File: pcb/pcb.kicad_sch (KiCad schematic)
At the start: 47 parts, among them J1 Power, Q1 Q_NPN_BCE, SW1 START, SW2 RESET, U1 PIC16F18346-P, U2 74HC595, U3 SCORE 1, U4 74HC595, U5 SCORE 1, U6 SSD1306

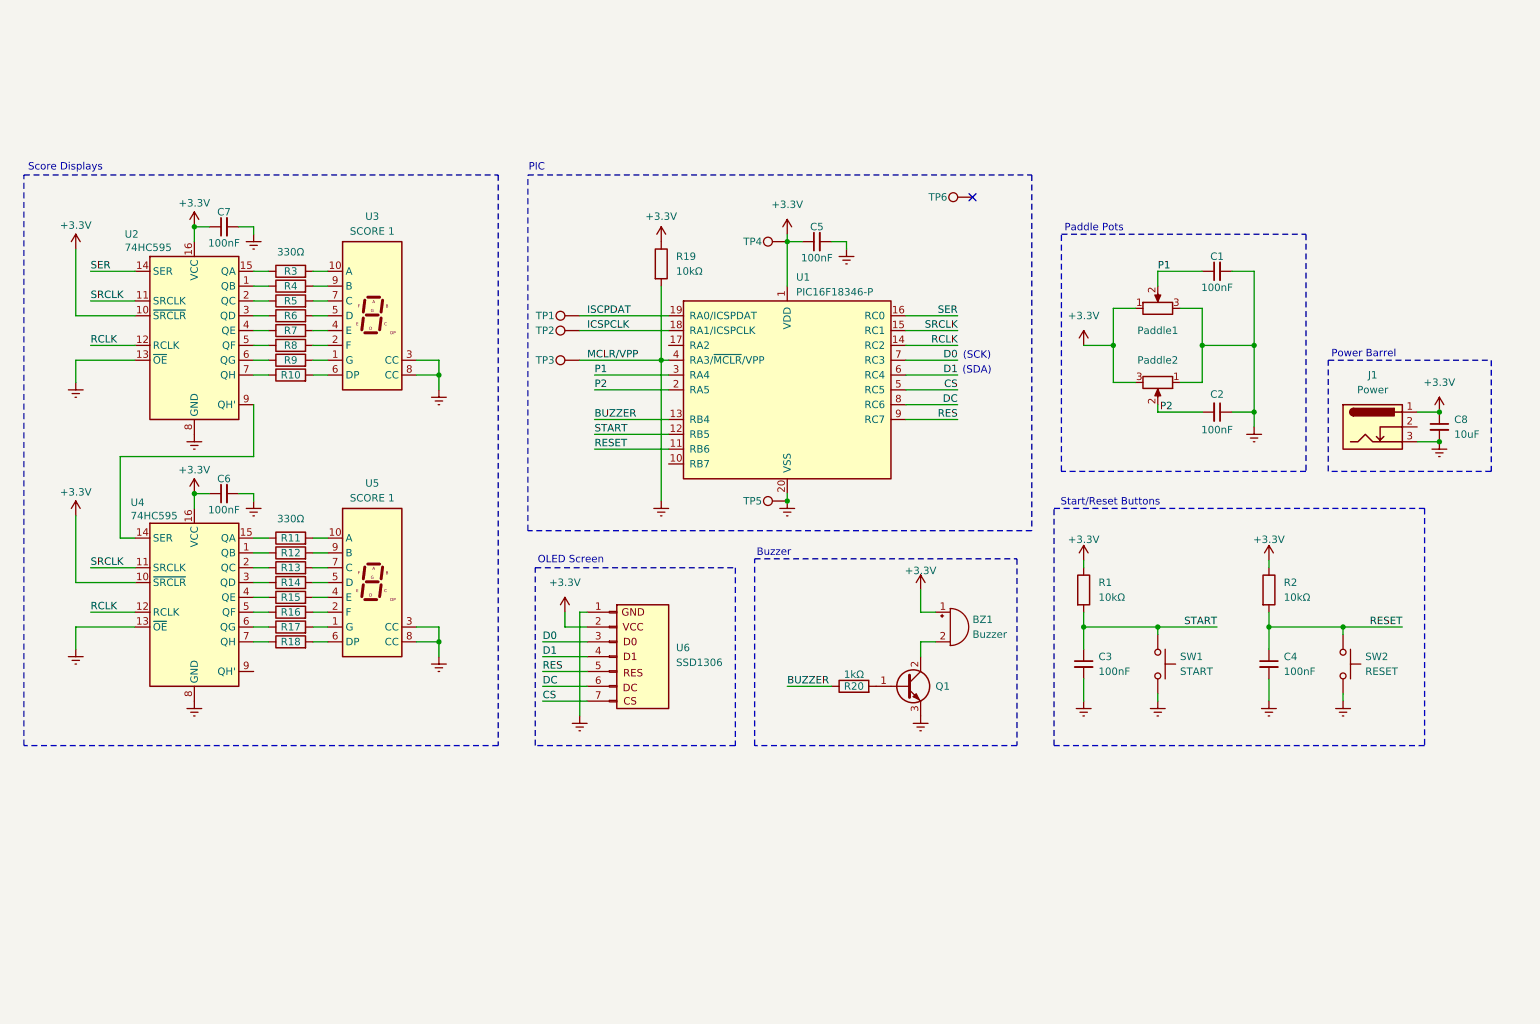
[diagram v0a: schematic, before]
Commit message: Assign footprints and start PCB
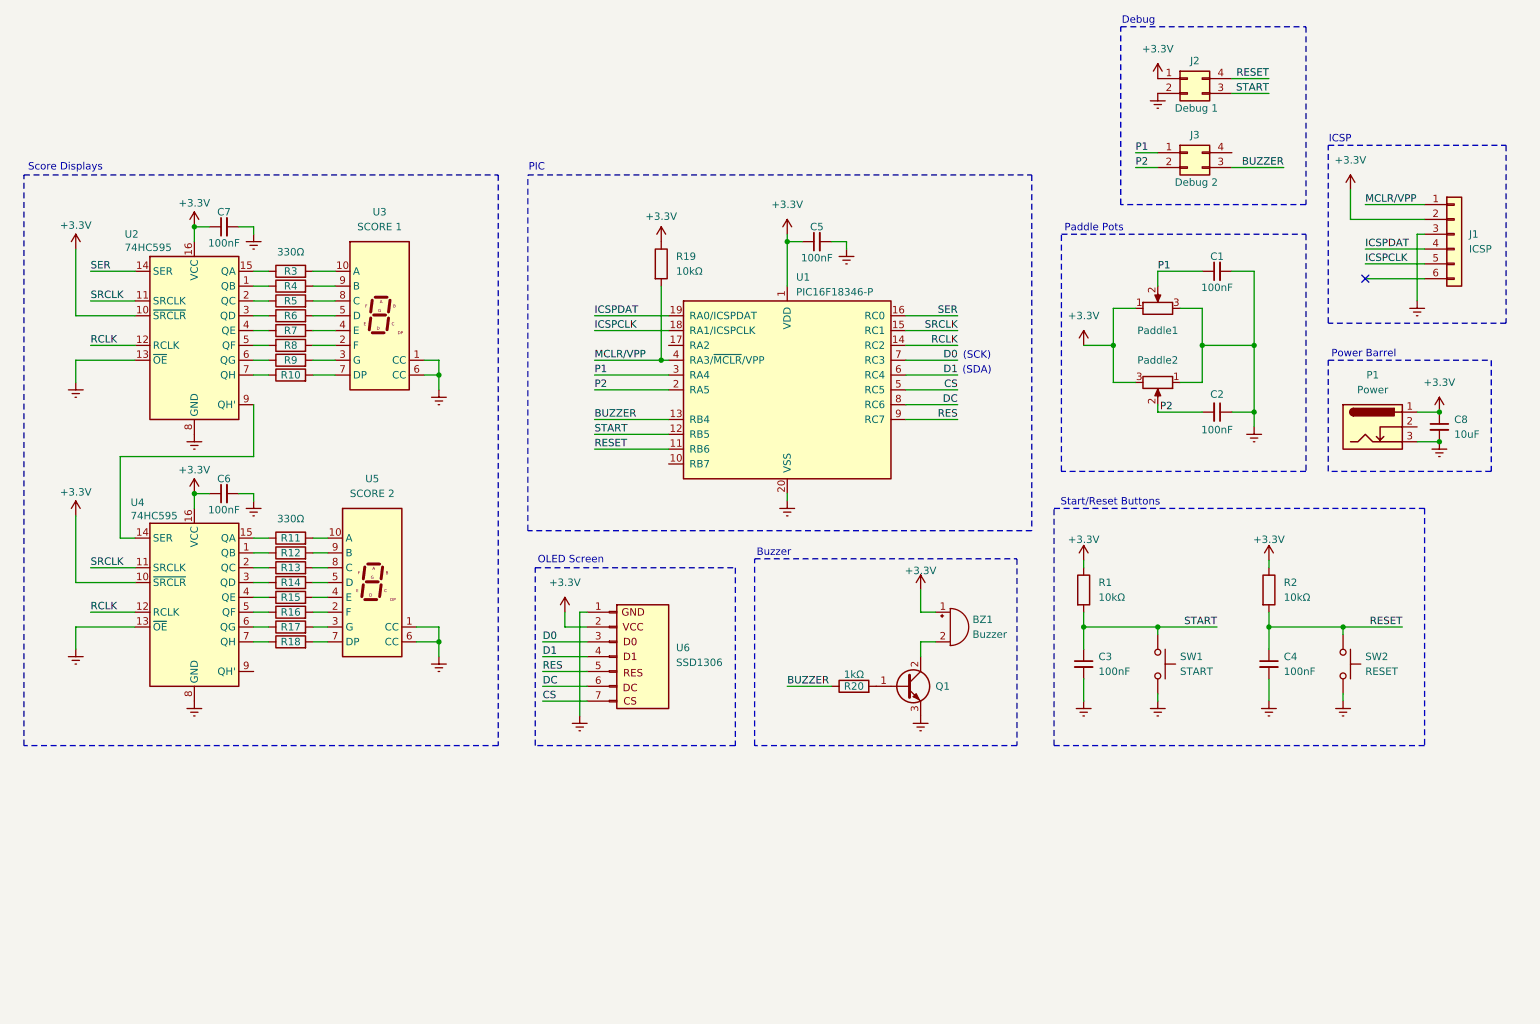
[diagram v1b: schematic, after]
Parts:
- removed TP1, TP2, TP3, TP4, TP5, TP6: TestPoint, symbol Connector:TestPoint
- added J1: ICSP, Connector_PinHeader_2.54mm:PinHeader_1x06_P2.54mm_Vertical, symbol Connector_Generic:Conn_01x06
- added J2: Debug 1, Connector_PinHeader_2.54mm:PinHeader_2x02_P2.54mm_Vertical, symbol Connector_Generic:Conn_02x02_Counter_Clockwise
- added J3: Debug 2, Connector_PinHeader_2.54mm:PinHeader_2x02_P2.54mm_Vertical, symbol Connector_Generic:Conn_02x02_Counter_Clockwise
- BZ1: footprint (none) -> Buzzer_Beeper:Buzzer_12x9.5RM7.6
- C1, C2, C3, C4, C5, C6, C7: footprint (none) -> Capacitor_THT:C_Disc_D5.0mm_W2.5mm_P5.00mm
- C8: footprint (none) -> Capacitor_THT:C_Radial_D5.0mm_H11.0mm_P2.00mm
- Paddle1, Paddle2: footprint (none) -> Potentiometer_THT:Potentiometer_Alps_RK09K_Single_Vertical
- Q1: footprint (none) -> Package_TO_SOT_THT:TO-92_Inline_Wide
- R1, R10, R11, R12, R13, R14, R15, R16, R17, R18, R19, R2, R20, R3, R4, R5, R6, R7, R8, R9: footprint (none) -> Resistor_THT:R_Axial_DIN0207_L6.3mm_D2.5mm_P10.16mm_Horizontal
- SW1, SW2: footprint (none) -> Button_Switch_THT:SW_PUSH-12mm
- U1: footprint Package_DIP:DIP-20_W7.62mm -> Package_DIP:DIP-20_W7.62mm_Socket
- U2, U4: footprint (none) -> Package_DIP:DIP-16_W7.62mm_LongPads
- U3: footprint Display_7Segment:Sx39-1xxxxx -> Display_7Segment:0.36in 3161AS
- U5: value SCORE 1 -> SCORE 2; footprint Display_7Segment:Sx39-1xxxxx -> Display_7Segment:0.36in 3161AS
- U6: footprint (none) -> Connector_PinSocket_2.54mm:PinSocket_1x07_P2.54mm_Vertical
- renumbered J1 to P1
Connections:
- net +3.3V: now also J1.2 (Pin_2), J2.1 (Pin_1)
- net BUZZER: now also J3.3 (Pin_3)
- net Earth: now also U3.1 (CC), U3.6 (CC), U5.1 (CC), U5.6 (CC), J1.3 (Pin_3), J2.2 (Pin_2); no longer R19.2, U1.4 (RA3/~{MCLR}/VPP), U3.3 (CC), U3.8 (CC), U5.3 (CC), U5.8 (CC)
- net ICSPCLK: now also J1.5 (Pin_5)
- net P1: now also J3.1 (Pin_1)
- net P2: now also J3.2 (Pin_2)
- net RESET: now also J2.4 (Pin_4)
- net START: now also J2.3 (Pin_3)
- net at R17.2: now also U5.3 (G); no longer U5.1 (G)
- net at R9.2: now also U3.3 (G); no longer U3.1 (G)
- net at R10.2: now also U3.7 (DP); no longer U3.6 (DP)
- net at R5.2: now also U3.8 (C); no longer U3.7 (C)
- net at R18.2: now also U5.7 (DP); no longer U5.6 (DP)
- net at R13.2: now also U5.8 (C); no longer U5.7 (C)
- net ISCPDAT renamed ICSPDAT
- net ICSPDAT: now also J1.4 (Pin_4)
- new net MCLR/VPP: J1.1 (Pin_1), R19.2, U1.4 (RA3/~{MCLR}/VPP)
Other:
- note added: "Debug"
- note added: "ICSP"

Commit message: Layout PCB
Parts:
- added D1: D_Small, Diode_THT:D_DO-35_SOD27_P7.62mm_Horizontal, symbol Device:D_Small
- U2, U4: footprint Package_DIP:DIP-16_W7.62mm_LongPads -> Package_DIP:DIP-16_W7.62mm_Socket_LongPads
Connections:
- net +3.3V: now also Paddle2.1, D1.1 (K); no longer Paddle2.3
- net Earth: now also Paddle2.3; no longer Paddle2.1
- net at BZ1.2 (-), Q1.2 (C): now also D1.2 (A)
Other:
- moved on the sheet: BZ1, C1, C2, C3, C4, C8, J1, J2, J3, P1, Paddle1, Paddle2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

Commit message: Hardware testing
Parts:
- removed Q1: Q_NPN_BCE, Package_TO_SOT_THT:TO-92_Inline_Wide, symbol Transistor_BJT:Q_NPN_BCE
- added Q1: BC107, Package_TO_SOT_THT:TO-92_Inline_Wide, symbol Transistor_BJT:BC107
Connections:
- net Earth: now also Q1.1 (E)
- net at R20.2: now also Q1.2 (B)
- net at BZ1.2 (-), D1.2 (A): now also Q1.3 (C)
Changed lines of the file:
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@@
 	)
 	(symbol
-		(lib_id "Transistor_BJT:Q_NPN_BCE")
-		(at 172.72 132.08 0)
-		(unit 1)
-		(exclude_from_sim no)
-		(in_bom yes)
-		(on_board yes)
-		(dnp no)
-		(property "Reference" "Q1"
-			(at 177.8 132.08 0)
-			(effects
-				(font
-					(size 1.27 1.27)
-				)
-				(justify left)
-			)
-		)
-		(property "Value" "Q_NPN_BCE"
-			(at 177.8 133.3499 0)
-			(effects
-				(font
-					(size 1.27 1.27)
-				)
-				(justify left)
-				(hide yes)
-			)
-		)
-		(property "Footprint" "Package_TO_SOT_THT:TO-92_Inline_Wide"
-			(at 177.8 129.54 0)
-			(effects
-				(font
-					(size 1.27 1.27)
-				)
-				(hide yes)
-			)
-		)
-		(property "Datasheet" "~"
-			(at 172.72 132.08 0)
-			(effects
-				(font
-					(size 1.27 1.27)
-				)
-				(hide yes)
-			)
-		)
-		(property "Description" "NPN transistor, base/collector/emitter"
-			(at 172.72 132.08 0)
-			(effects
-				(font
-					(size 1.27 1.27)
-				)
-				(hide yes)
-			)
-		)
-		(pin "2"
-		)
-		(pin "1"
-		)
-		(pin "3"
-		)
-		(instances
-			(project "pcb"
-				(path "/095fd1c6-3a4d-4d16-977e-3ab207ce523d"
-					(reference "Q1")
-					(unit 1)
-				)
-			)
-		)
-	)
-	(symbol
 		(lib_id "Device:R")
 		(at 68.58 60.96 90)
@@
 					(unit 1)
 				)
+			)
+		)
+	)
+	(symbol
+		(lib_id "Transistor_BJT:BC107")
+		(at 172.72 132.08 0)
+		(unit 1)
+		(exclude_from_sim no)
+		(in_bom yes)
+		(on_board yes)
+		(dnp no)
+		(fields_autoplaced yes)
+		(property "Reference" "Q1"
+			(at 177.8 130.8099 0)
+			(effects
+				(font
+					(size 1.27 1.27)
+				)
+				(justify left)
+			)
+		)
+		(property "Value" "BC107"
+			(at 177.8 133.3499 0)
+			(effects
+				(font
+					(size 1.27 1.27)
+				)
+				(justify left)
+			)
+		)
+		(property "Footprint" "Package_TO_SOT_THT:TO-92_Inline_Wide"
+			(at 177.8 133.985 0)
+			(effects
+				(font
+					(size 1.27 1.27)
+					(italic yes)
+				)
+				(justify left)
+				(hide yes)
+			)
+		)
+		(property "Datasheet" "http://www.b-kainka.de/Daten/Transistor/BC108.pdf"
+			(at 172.72 132.08 0)
+			(effects
+				(font
+					(size 1.27 1.27)
+				)
+				(justify left)
+				(hide yes)
+			)
+		)
+		(property "Description" "0.1A Ic, 50V Vce, Low Noise General Purpose NPN Transistor, TO-18"
+			(at 172.72 132.08 0)
+			(effects
+				(font
+					(size 1.27 1.27)
+				)
+				(hide yes)
+			)
+		)
+		(pin "3"
+		)
+		(pin "1"
+		)
+		(pin "2"
+		)
+		(instances
+			(project ""
+				(path "/095fd1c6-3a4d-4d16-977e-3ab207ce523d"
+					(reference "Q1")
+					(unit 1)
+				)

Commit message: Route PCB
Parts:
- added C9: 1uF, Capacitor_THT:C_Radial_D4.0mm_H7.0mm_P1.50mm, symbol Device:C_Small
- added U7: MCP1700x-330xxTO, Package_TO_SOT_THT:TO-92_Inline, symbol Regulator_Linear:MCP1700x-330xxTO
- C8: value 10uF -> 1uF; footprint Capacitor_THT:C_Radial_D5.0mm_H11.0mm_P2.00mm -> Capacitor_THT:C_Radial_D4.0mm_H7.0mm_P1.50mm
- Q1: value BC107 -> 2N2222
- R11, R3: value 330Ω -> 220Ω
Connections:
- net +3.3V: now also C9.1, U7.3 (VO); no longer C8.1, P1.1
- net Earth: now also P1.2, C9.2, U7.1 (GND); no longer P1.3
- net P1: now also U1.2 (RA5); no longer U1.3 (RA4)
- net P2: now also U1.3 (RA4); no longer U1.2 (RA5)
- net VIN: now reaches J3.4 (Pin_4)
- net VIN: now also C8.1, P1.1, U7.2 (VI)
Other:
- moved on the sheet: C8, P1

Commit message: Finish 3D model and render
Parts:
- added H1, H2, H3, H4: MountingHole, MountingHole:MountingHole_2.2mm_M2, symbol Mechanical:MountingHole
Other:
- note added: "Mounting Holes"
